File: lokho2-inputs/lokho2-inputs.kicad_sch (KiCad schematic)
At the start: 60 parts, among them J1 SWITCHES, Q1 BC846, SW1 SW_DIP_x04, U1 74HC85, U2 MCP23S17_SP, U3 74AHC04, U4 74AHC04, U5 74AHC04

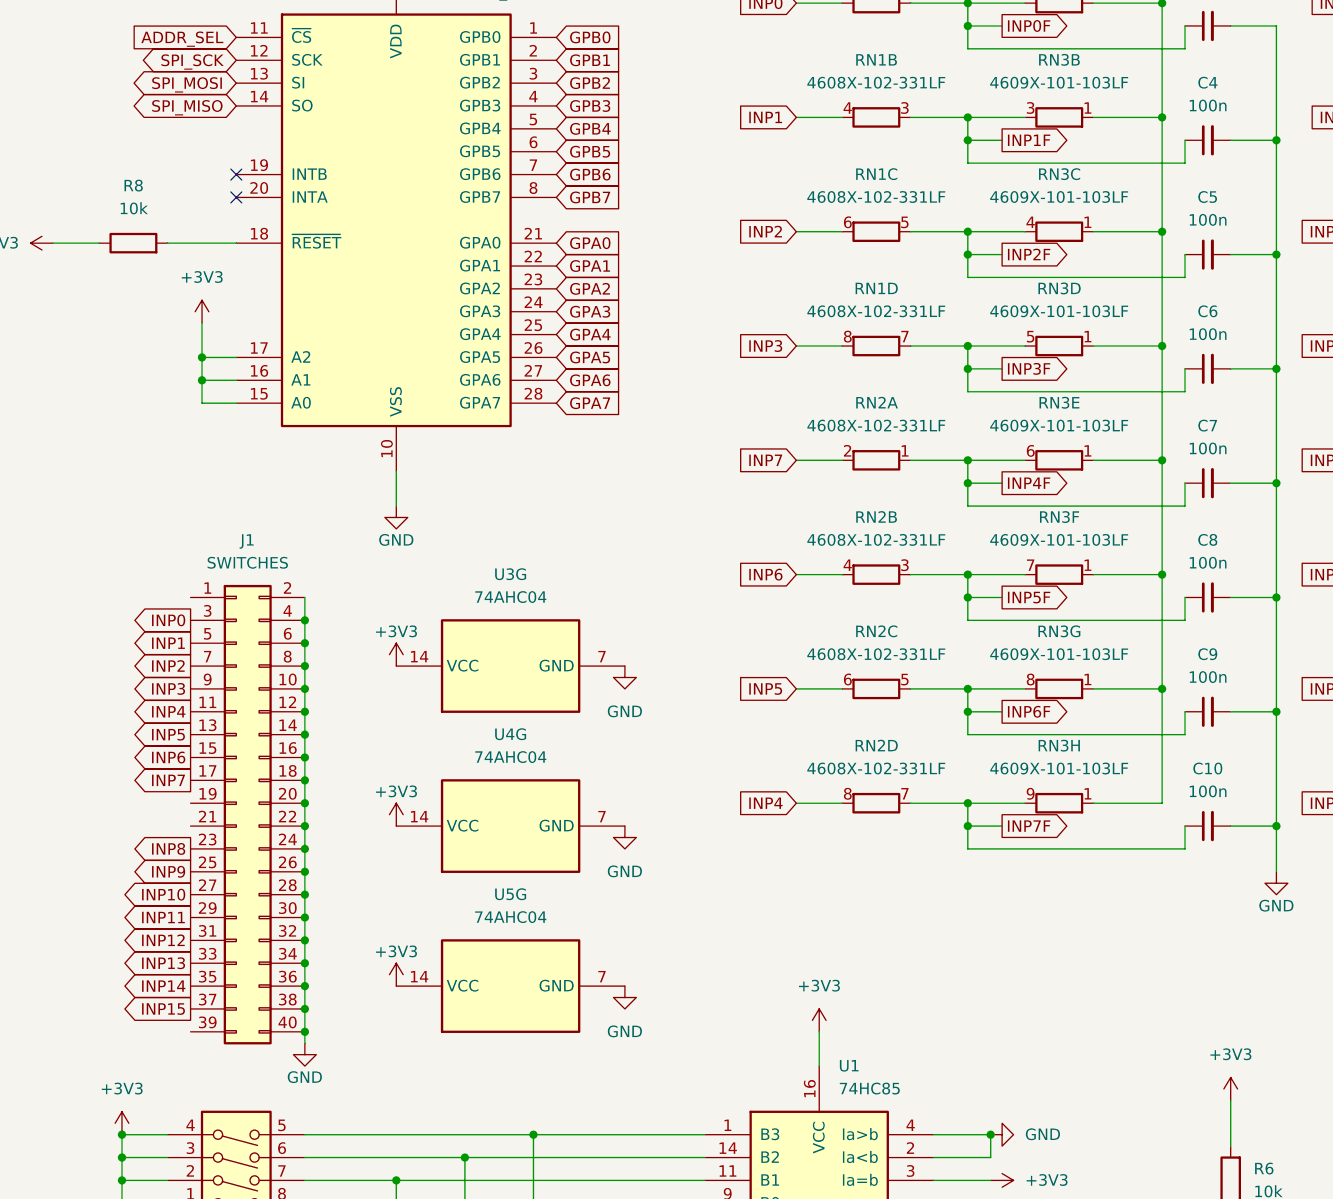
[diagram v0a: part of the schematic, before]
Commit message: added INT-GP connection option
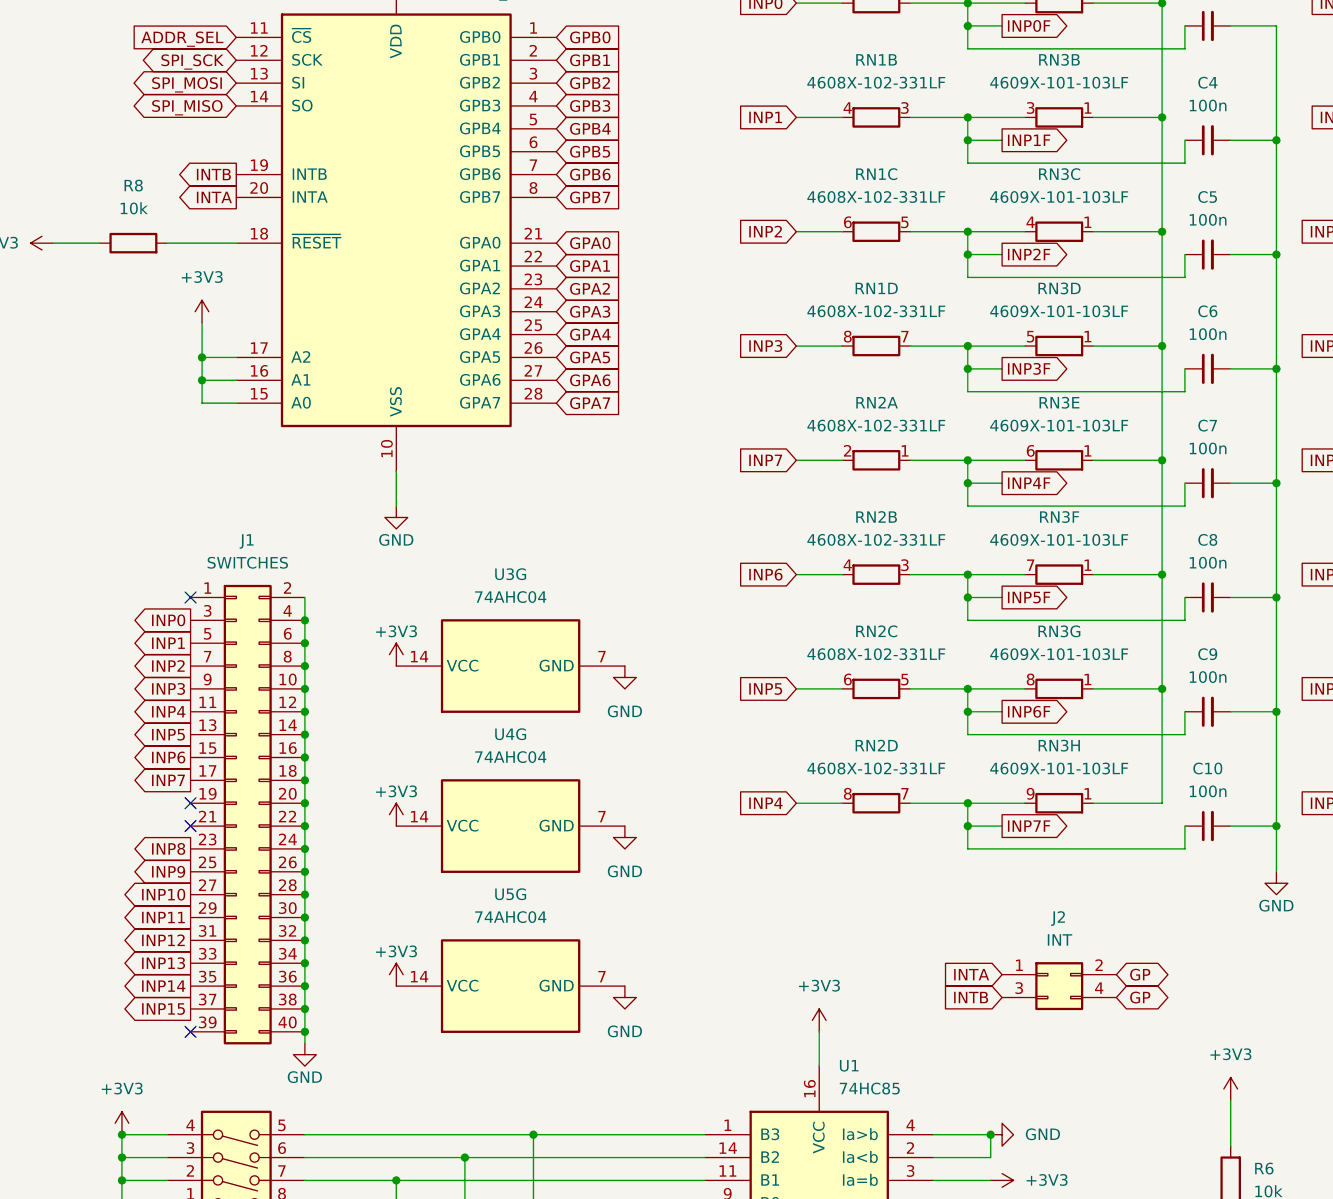
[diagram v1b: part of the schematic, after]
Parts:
- added J2: INT, Connector_PinHeader_2.54mm:PinHeader_2x02_P2.54mm_Vertical, symbol Connector_Generic:Conn_02x02_Odd_Even
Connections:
- net GP: now also J2.2 (Pin_2), J2.4 (Pin_4)
- net INTB: now reaches U2.19 (INTB)
- net INTB: now also J2.3 (Pin_3)
- net INTA: now reaches U2.20 (INTA)
- net INTA: now also J2.1 (Pin_1)
- no-connect marks 4 -> 6
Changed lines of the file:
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@@
 	)
 	(no_connect
-		(at 45.72 52.07)
+		(at 40.64 124.46)
 	)
 	(no_connect
@@
 	)
 	(no_connect
-		(at 45.72 54.61)
+		(at 40.64 121.92)
+	)
+	(no_connect
+		(at 40.64 99.06)
+	)
+	(no_connect
+		(at 40.64 147.32)
 	)
 	(wire
@@
 		)
 	)
+	(global_label "INTA"
+		(shape output)
+		(at 45.72 54.61 180)
+		(fields_autoplaced yes)
+		(effects
+			(font
+				(size 1.27 1.27)
+			)
+			(justify right)
+		)
+		(property "Intersheetrefs" "${INTERSHEET_REFS}"
+			(at 38.7433 54.61 0)
+			(effects
+				(font
+					(size 1.27 1.27)
+				)
+				(justify right)
+				(hide yes)
+			)
+		)
+	)
 	(global_label "GPA6"
 		(shape input)
@@
 		)
 	)
+	(global_label "INTB"
+		(shape input)
+		(at 130.81 143.51 180)
+		(fields_autoplaced yes)
+		(effects
+			(font
+				(size 1.27 1.27)
+			)
+			(justify right)
+		)
+		(property "Intersheetrefs" "${INTERSHEET_REFS}"
+			(at 123.6519 143.51 0)
+			(effects
+				(font
+					(size 1.27 1.27)
+				)
+				(justify right)
+				(hide yes)
+			)
+		)
+	)
 	(global_label "SPI_S0"
 		(shape bidirectional)
@@
 		)
 	)
+	(global_label "INTB"
+		(shape output)
+		(at 45.72 52.07 180)
+		(fields_autoplaced yes)
+		(effects
+			(font
+				(size 1.27 1.27)
+			)
+			(justify right)
+		)
+		(property "Intersheetrefs" "${INTERSHEET_REFS}"
+			(at 38.5619 52.07 0)
+			(effects
+				(font
+					(size 1.27 1.27)
+				)
+				(justify right)
+				(hide yes)
+			)
+		)
+	)
 	(global_label "GPA3"
 		(shape output)
@@
 	(global_label "GP"
 		(shape bidirectional)
+		(at 143.51 143.51 0)
+		(fields_autoplaced yes)
+		(effects
+			(font
+				(size 1.27 1.27)
+			)
+			(justify left)
+		)
+		(property "Intersheetrefs" "${INTERSHEET_REFS}"
+			(at 150.1465 143.51 0)
+			(effects
+				(font
+					(size 1.27 1.27)
+				)
+				(justify left)
+				(hide yes)
+			)
+		)
+	)
+	(global_label "GP"
+		(shape bidirectional)
 		(at 241.3 157.48 180)
 		(fields_autoplaced yes)
@@
 		)
 	)
+	(global_label "INTA"
+		(shape input)
+		(at 130.81 140.97 180)
+		(fields_autoplaced yes)
+		(effects
+			(font
+				(size 1.27 1.27)
+			)
+			(justify right)
+		)
+		(property "Intersheetrefs" "${INTERSHEET_REFS}"
+			(at 123.8333 140.97 0)
+			(effects
+				(font
+					(size 1.27 1.27)
+				)
+				(justify right)
+				(hide yes)
+			)
+		)
+	)
 	(global_label "GPB7"
 		(shape input)
@@
 		)
 	)
+	(global_label "GP"
+		(shape bidirectional)
+		(at 143.51 140.97 0)
+		(fields_autoplaced yes)
+		(effects
+			(font
+				(size 1.27 1.27)
+			)
+			(justify left)
+		)
+		(property "Intersheetrefs" "${INTERSHEET_REFS}"
+			(at 150.1465 140.97 0)
+			(effects
+				(font
+					(size 1.27 1.27)
+				)
+				(justify left)
+				(hide yes)
+			)
+		)
+	)
 	(global_label "GPB2"
 		(shape input)
@@
 					(unit 1)
 				)
+			)
+		)
+	)
+	(symbol
+		(lib_id "Connector_Generic:Conn_02x02_Odd_Even")
+		(at 135.89 140.97 0)
+		(unit 1)
+		(exclude_from_sim no)
+		(in_bom yes)
+		(on_board yes)
+		(dnp no)
+		(fields_autoplaced yes)
+		(property "Reference" "J2"
+			(at 137.16 134.62 0)
+			(effects
+				(font
+					(size 1.27 1.27)
+				)
+			)
+		)
+		(property "Value" "INT"
+			(at 137.16 137.16 0)
+			(effects
+				(font
+					(size 1.27 1.27)
+				)
+			)
+		)
+		(property "Footprint" "Connector_PinHeader_2.54mm:PinHeader_2x02_P2.54mm_Vertical"
+			(at 135.89 140.97 0)
+			(effects
+				(font
+					(size 1.27 1.27)
+				)
+				(hide yes)
+			)
+		)
+		(property "Datasheet" "~"
+			(at 135.89 140.97 0)
+			(effects
+				(font
+					(size 1.27 1.27)
+				)
+				(hide yes)
+			)
+		)
+		(property "Description" "Generic connector, double row, 02x02, odd/even pin numbering scheme (row 1 odd numbers, row 2 even numbers), script generated (kicad-library-utils/schlib/autogen/connector/)"
+			(at 135.89 140.97 0)
+			(effects
+				(font
+					(size 1.27 1.27)
+				)
+				(hide yes)
+			)
+		)
+		(pin "1"
+		)
+		(pin "3"
+		)
+		(pin "2"
+		)
+		(pin "4"
+		)
+		(instances
+			(project ""
+				(path "/b58ba24b-eb25-4f2b-8ecb-c8d26726374c"
+					(reference "J2")
+					(unit 1)
+				)
